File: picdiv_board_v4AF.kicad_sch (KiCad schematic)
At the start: 54 parts, among them J1 DC-Input, J10 PPS_B, J11 PPS_B, J2 MountingHole_M2.5, J3 MountingHole_M2.5, J4 TEST_1PPS, J5 Conn_01x06, J8 PPS_A, J9 PPS_A, SW1 SW_DIP_x03, U1 LT1963AxST-3.3, U2 LT1963AxST-3.3, U3 PIC12F675-xSN, U4 LTC6993xS6-1, U5 IDT5PB1108, U6 IDT5PB1108

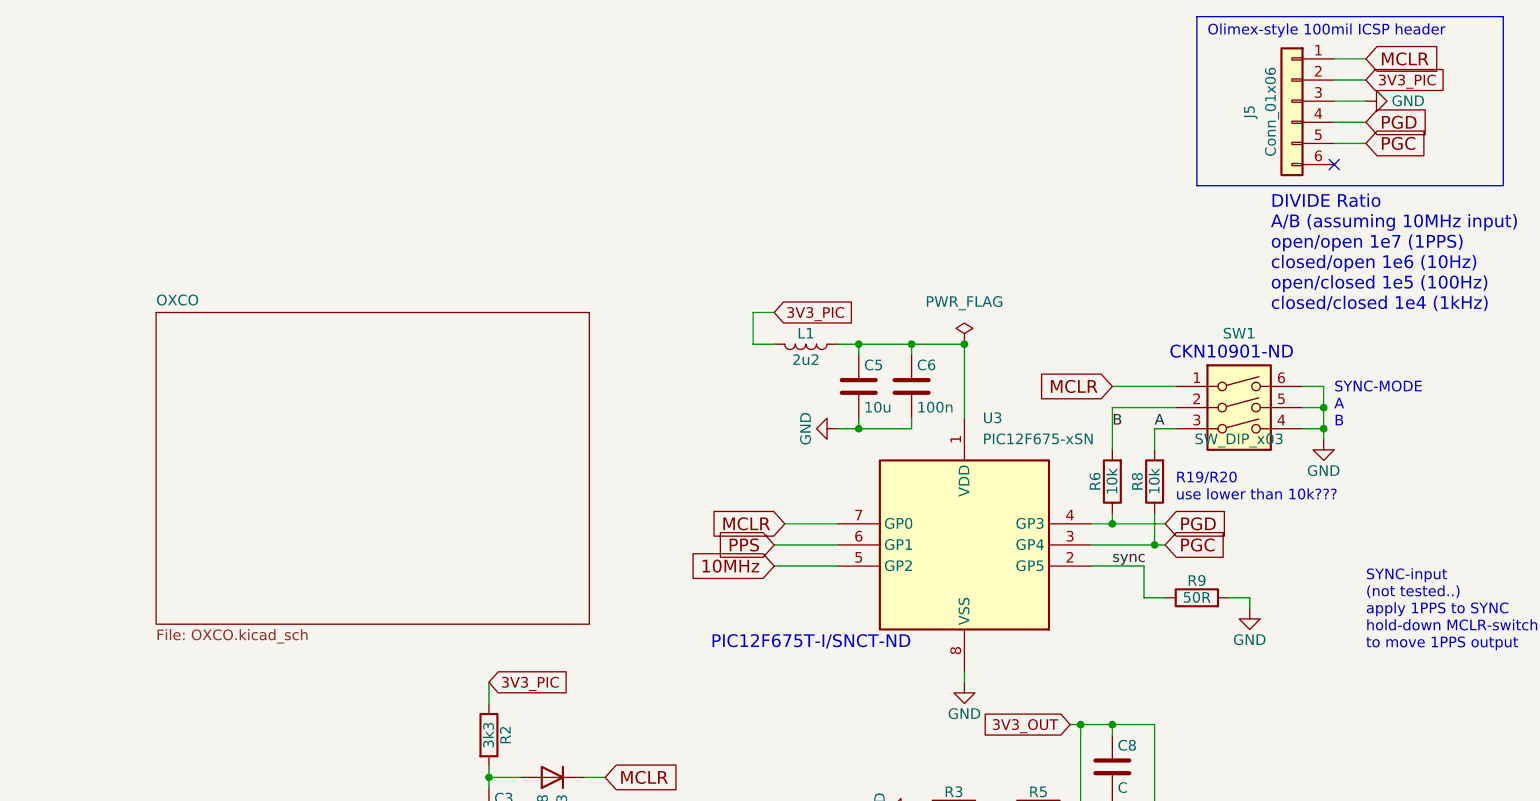
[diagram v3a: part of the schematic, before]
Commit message: Getting closer on parts placement.
Fixed a few backwards parts caused by newer libraries.  Several are mirrors of what was in the orginal symbol.  I wonder if he made his own to make the schematic clearer.
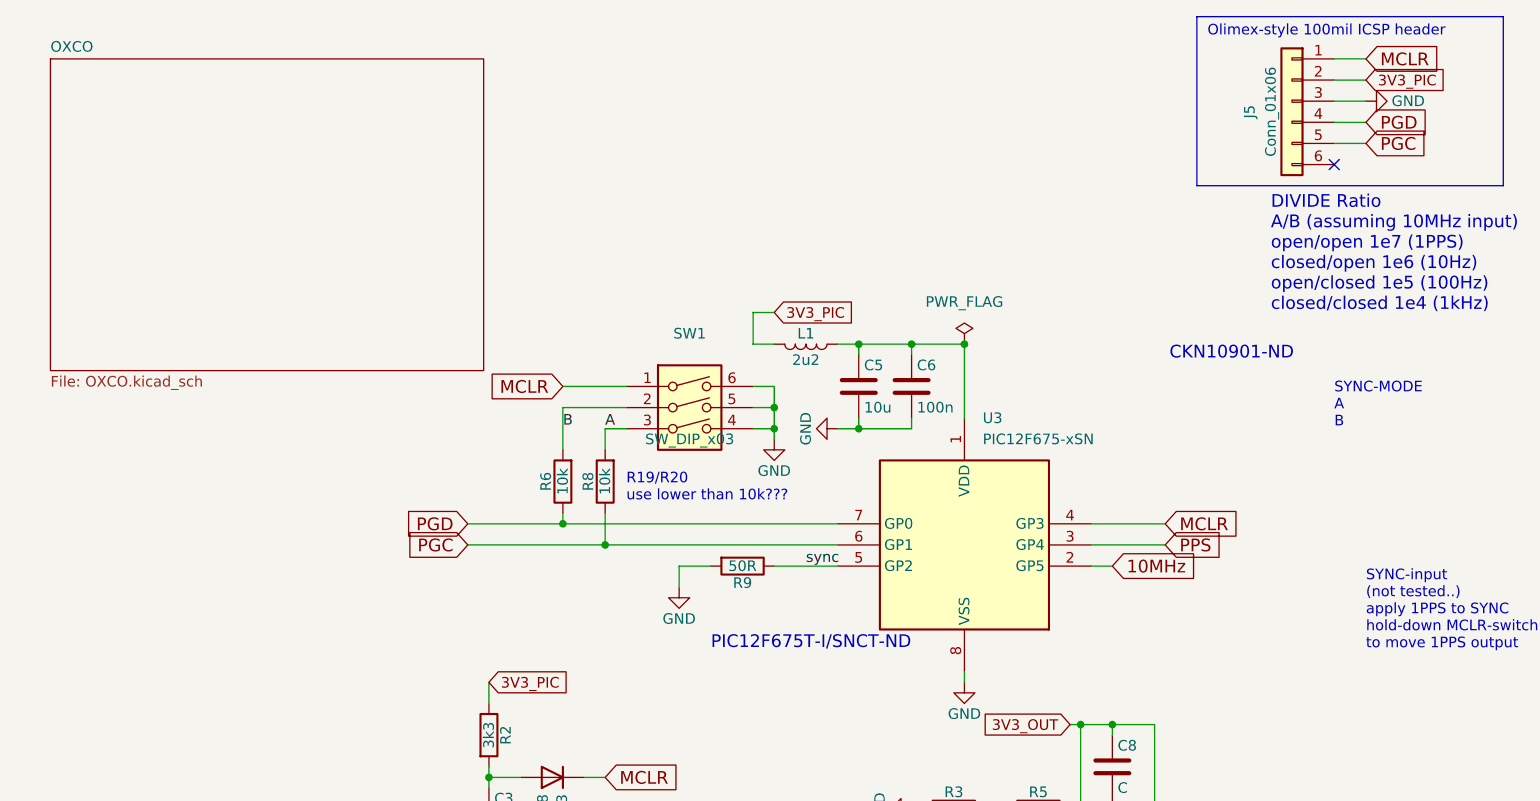
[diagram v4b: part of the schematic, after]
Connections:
- net 10MHz: now also U3.2 (GP5); no longer U3.5 (GP2)
- net MCLR: now also U3.4 (GP3); no longer U3.7 (GP0)
- net PGC: now also U3.6 (GP1); no longer U3.3 (GP4)
- net PGD: now also U3.7 (GP0); no longer U3.4 (GP3)
- net PPS: now also U3.3 (GP4); no longer U3.6 (GP1)
- net sync: now also U3.5 (GP2); no longer U3.2 (GP5)
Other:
- moved on the sheet: R9

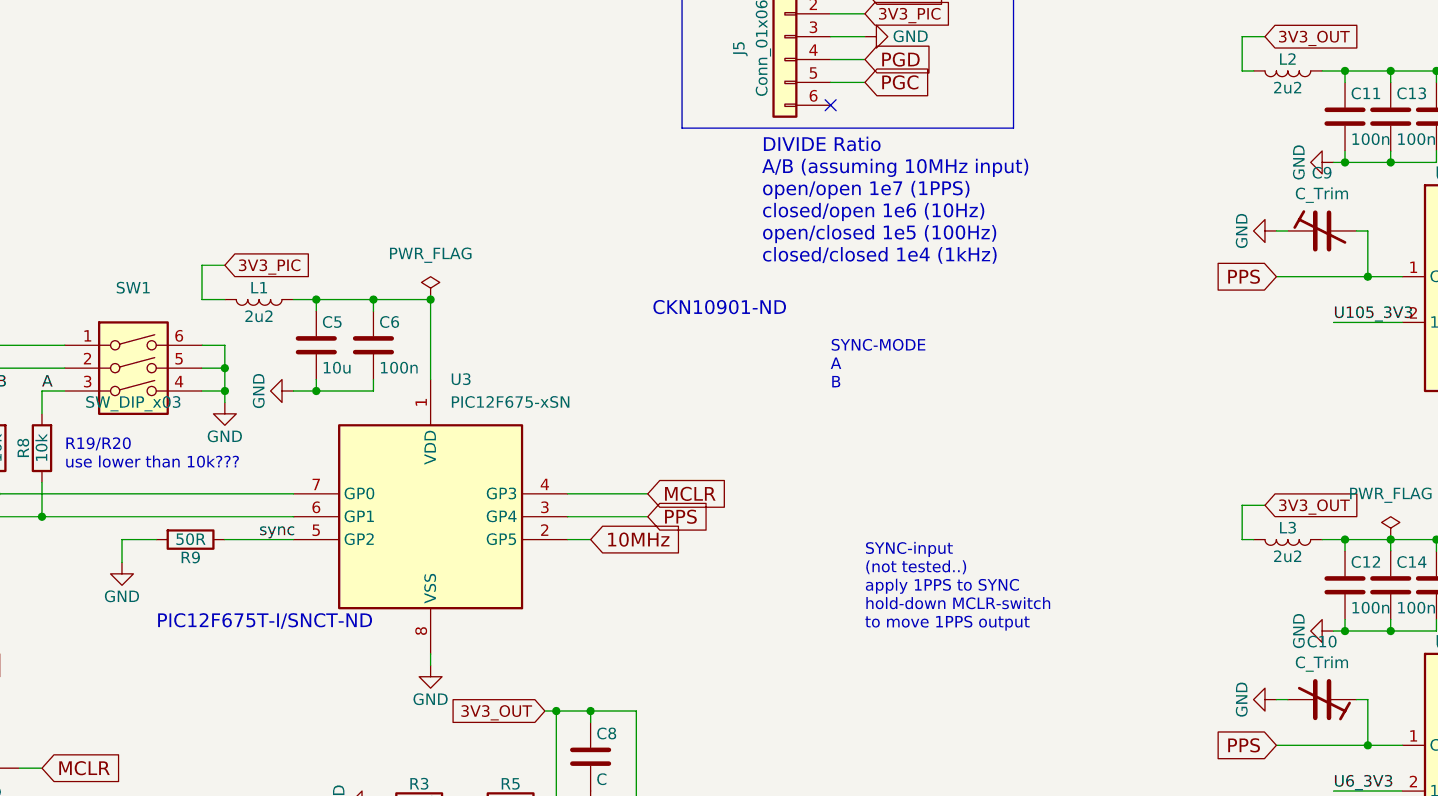
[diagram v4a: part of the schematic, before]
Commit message: Redraw for clarity.   Add LCSC parts.
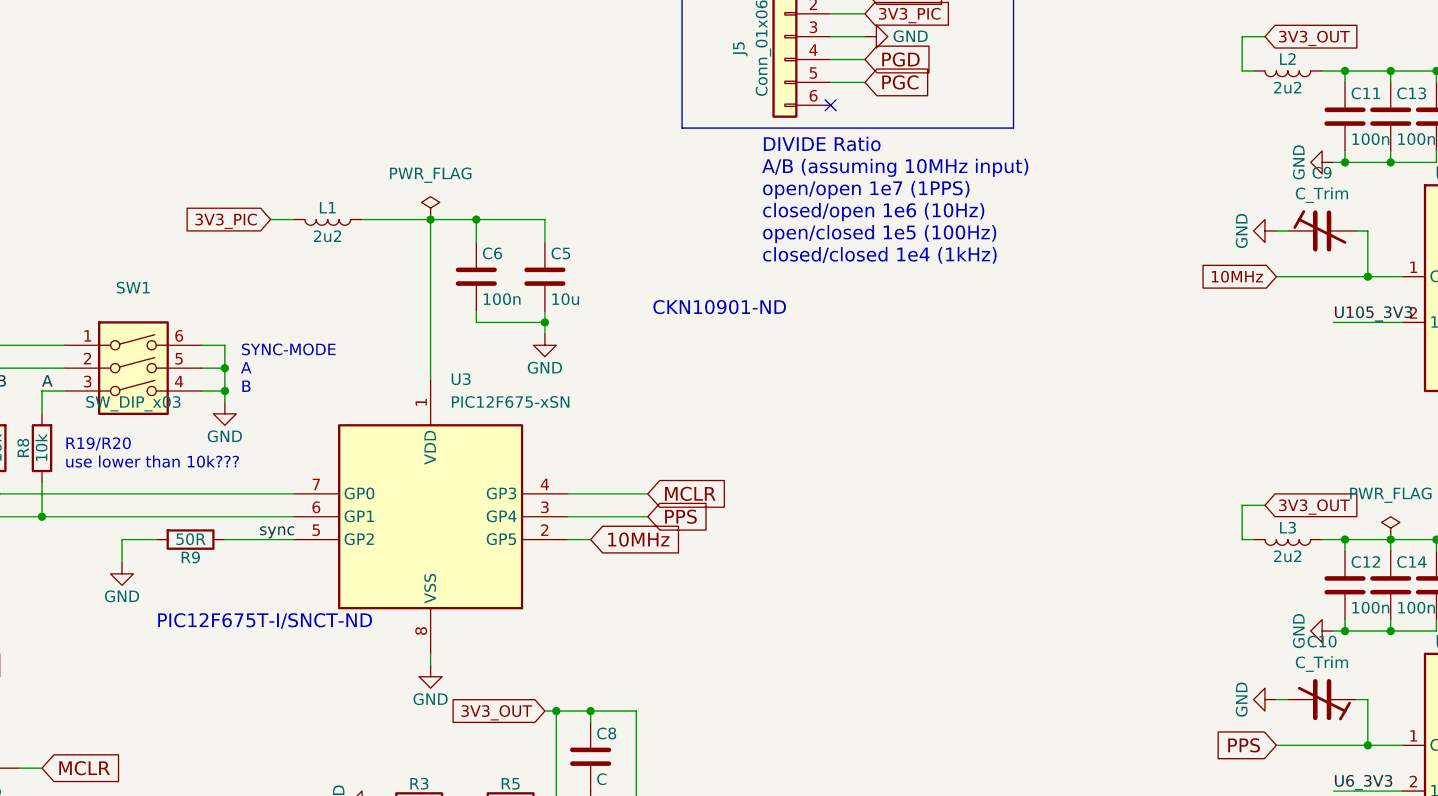
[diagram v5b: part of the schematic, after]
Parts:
- C11, C13, C6: LCSC (none) -> C49678; MPN (none) -> CC0805KRX7R9BB104
- C12, C14, C15, C16: LCSC (none) -> C49678
- C5: MPN (none) -> CL21A106KAYNNNE
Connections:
- net 10MHz: now also C9.2, U5.1 (CLKIN)
- net PPS: no longer C9.2, U5.1 (CLKIN)
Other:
- note removed: "SYNC-input (not tested..) apply 1PPS to SYNC hold-down MCLR-switch to move 1PPS output"
- moved on the sheet: C5, C6, L1
